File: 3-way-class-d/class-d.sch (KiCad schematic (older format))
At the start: 88 parts

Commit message: Make it a bit prettier
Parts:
- R? (x4): value 10 -> 3,3
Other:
- moved on the sheet: D?, Q?, R?
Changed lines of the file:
@@
 L R R?
 U 1 1 572BC593
-P 1400 3100
-F 0 "R?" V 1480 3100 50  0000 C CNN
-F 1 "0" V 1400 3100 50  0000 C CNN
-F 2 "" V 1330 3100 30  0000 C CNN
-F 3 "" H 1400 3100 30  0000 C CNN
-	1    1400 3100
+P 2150 3500
+F 0 "R?" V 2230 3500 50  0000 C CNN
+F 1 "0" V 2150 3500 50  0000 C CNN
+F 2 "" V 2080 3500 30  0000 C CNN
+F 3 "" H 2150 3500 30  0000 C CNN
+	1    2150 3500
 	0    1    1    0
 $EndComp
@@
 L GNDPWR #PWR?
 U 1 1 572BC8E0
-P 1100 3200
-F 0 "#PWR?" H 1100 3000 50  0001 C CNN
-F 1 "GNDPWR" H 1100 3070 50  0000 C CNN
-F 2 "" H 1100 3150 60  0000 C CNN
-F 3 "" H 1100 3150 60  0000 C CNN
-	1    1100 3200
+P 1850 3600
+F 0 "#PWR?" H 1850 3400 50  0001 C CNN
+F 1 "GNDPWR" H 1850 3470 50  0000 C CNN
+F 2 "" H 1850 3550 60  0000 C CNN
+F 3 "" H 1850 3550 60  0000 C CNN
+	1    1850 3600
 	0    1    1    0
 $EndComp
@@
 L R R?
 U 1 1 572BC605
-P 1400 3300
-F 0 "R?" V 1480 3300 50  0000 C CNN
-F 1 "22,1k" V 1400 3300 50  0000 C CNN
-F 2 "" V 1330 3300 30  0000 C CNN
-F 3 "" H 1400 3300 30  0000 C CNN
-	1    1400 3300
+P 2150 3700
+F 0 "R?" V 2230 3700 50  0000 C CNN
+F 1 "22,1k" V 2150 3700 50  0000 C CNN
+F 2 "" V 2080 3700 30  0000 C CNN
+F 3 "" H 2150 3700 30  0000 C CNN
+	1    2150 3700
 	0    1    1    0
 $EndComp
@@
 L BC857 Q?
 U 1 1 572BD9A9
-P 7250 4600
-F 0 "Q?" H 7450 4675 50  0000 L CNN
-F 1 "BC857" H 7450 4600 50  0000 L CNN
-F 2 "SOT-23" H 7450 4525 50  0000 L CIN
-F 3 "" H 7250 4600 50  0000 L CNN
-	1    7250 4600
+P 7300 4600
+F 0 "Q?" H 7500 4675 50  0000 L CNN
+F 1 "BC857" H 7500 4600 50  0000 L CNN
+F 2 "SOT-23" H 7500 4525 50  0000 L CIN
+F 3 "" H 7300 4600 50  0000 L CNN
+	1    7300 4600
 	1    0    0    -1
 $EndComp
@@
 L LED D?
 U 1 1 572BDA25
-P 7550 4400
-F 0 "D?" H 7550 4500 50  0000 C CNN
-F 1 "LED" H 7550 4300 50  0000 C CNN
-F 2 "" H 7550 4400 60  0000 C CNN
-F 3 "" H 7550 4400 60  0000 C CNN
-F 4 "Red" H 7550 4400 60  0001 C CNN "Color"
-	1    7550 4400
+P 7600 4400
+F 0 "D?" H 7600 4500 50  0000 C CNN
+F 1 "LED" H 7600 4300 50  0000 C CNN
+F 2 "" H 7600 4400 60  0000 C CNN
+F 3 "" H 7600 4400 60  0000 C CNN
+F 4 "Red" H 7600 4400 60  0001 C CNN "Color"
+	1    7600 4400
 	-1   0    0    1
 $EndComp
@@
 L GNDPWR #PWR?
 U 1 1 572BDA9C
-P 8050 4400
-F 0 "#PWR?" H 8050 4200 50  0001 C CNN
-F 1 "GNDPWR" H 8050 4270 50  0000 C CNN
-F 2 "" H 8050 4350 60  0000 C CNN
-F 3 "" H 8050 4350 60  0000 C CNN
-	1    8050 4400
+P 8100 4400
+F 0 "#PWR?" H 8100 4200 50  0001 C CNN
+F 1 "GNDPWR" H 8100 4270 50  0000 C CNN
+F 2 "" H 8100 4350 60  0000 C CNN
+F 3 "" H 8100 4350 60  0000 C CNN
+	1    8100 4400
 	0    -1   -1   0
 $EndComp
@@
 L R R?
 U 1 1 572BDBE6
-P 7900 4400
-F 0 "R?" V 7980 4400 50  0000 C CNN
-F 1 "332" V 7900 4400 50  0000 C CNN
-F 2 "" V 7830 4400 30  0000 C CNN
-F 3 "" H 7900 4400 30  0000 C CNN
-	1    7900 4400
+P 7950 4400
+F 0 "R?" V 8030 4400 50  0000 C CNN
+F 1 "332" V 7950 4400 50  0000 C CNN
+F 2 "" V 7880 4400 30  0000 C CNN
+F 3 "" H 7950 4400 30  0000 C CNN
+	1    7950 4400
 	0    1    -1   0
 $EndComp
@@
 L +3.3V #PWR?
 U 1 1 572BE227
-P 7350 4800
-F 0 "#PWR?" H 7350 4650 50  0001 C CNN
-F 1 "+3.3V" H 7350 4940 50  0000 C CNN
-F 2 "" H 7350 4800 60  0000 C CNN
-F 3 "" H 7350 4800 60  0000 C CNN
-	1    7350 4800
+P 7400 4800
+F 0 "#PWR?" H 7400 4650 50  0001 C CNN
+F 1 "+3.3V" H 7400 4940 50  0000 C CNN
+F 2 "" H 7400 4800 60  0000 C CNN
+F 3 "" H 7400 4800 60  0000 C CNN
+	1    7400 4800
 	-1   0    0    1
 $EndComp
-Text Notes 7150 4300 0    60   ~ 0
+Text Notes 7200 4300 0    60   ~ 0
 valid
-Text GLabel 7600 3700 2    60   Output ~ 0
+Text GLabel 7600 3500 2    60   Output ~ 0
 SUB-PWM+
-Text GLabel 7600 3900 2    60   Output ~ 0
+Text GLabel 7600 3650 2    60   Output ~ 0
 SUB-PWM-
-Text GLabel 7600 4100 2    60   Output ~ 0
+Text GLabel 7600 3800 2    60   Output ~ 0
 SUB-RESET
 $Comp
 L R R?
 U 1 1 572BECAA
-P 7250 4100
-F 0 "R?" V 7330 4100 50  0000 C CNN
-F 1 "47" V 7250 4100 50  0000 C CNN
-F 2 "" V 7180 4100 30  0000 C CNN
-F 3 "" H 7250 4100 30  0000 C CNN
-	1    7250 4100
+P 7250 3800
+F 0 "R?" V 7330 3800 50  0000 C CNN
+F 1 "47" V 7250 3800 50  0000 C CNN
+F 2 "" V 7180 3800 30  0000 C CNN
+F 3 "" H 7250 3800 30  0000 C CNN
+	1    7250 3800
 	0    -1   1    0
 $EndComp
@@
 Text GLabel 7650 5300 2    60   Input ~ 0
 MCLK
-Text GLabel 7650 5100 2    60   Output ~ 0
+Text GLabel 7600 3950 2    60   Input ~ 0
 BKND-ERR
 $Comp
@@
 Connection ~ 3850 5950
 Wire Wire Line
-	2850 4400 2450 4400
-Wire Wire Line
-	2450 4400 2450 3650
-Wire Wire Line
-	2450 3650 1800 3650
-Wire Wire Line
-	1800 3650 1800 1300
+	2450 4400 2850 4400
+Wire Wire Line
+	2450 1450 2450 4400
 Wire Notes Line
 	2400 1300 500  1300
@@
 Wire Notes Line
 	500  650  2400 650
-Wire Notes Line
-	2500 650  2500 1300
 Wire Wire Line
 	2050 6350 4050 6350
@@
 	2850 4500 2350 4500
 Wire Wire Line
-	1100 3200 1250 3200
+	1850 3600 2000 3600
 Wire Wire Line
 	2850 4300 2500 4300
 Wire Wire Line
-	1250 3100 1250 3300
-Connection ~ 1250 3200
-Wire Wire Line
-	1550 3300 2500 3300
-Wire Wire Line
-	2500 3300 2500 4300
+	2000 3500 2000 3700
+Connection ~ 2000 3600
 Wire Wire Line
 	2850 4200 2550 4200
-Wire Wire Line
-	2550 4200 2550 3100
-Wire Wire Line
-	2550 3100 1550 3100
-Wire Wire Line
-	5950 4600 7050 4600
 Connection ~ 6400 4250
 Wire Notes Line
-	7100 4200 7100 5000
-Wire Notes Line
-	7100 5000 8300 5000
-Wire Notes Line
-	8300 5000 8300 4200
-Wire Notes Line
-	8300 4200 7100 4200
-Wire Wire Line
-	6950 4100 6950 4600
-Connection ~ 6950 4600
-Wire Wire Line
-	5950 4500 6850 4500
-Wire Wire Line
-	6850 4500 6850 3900
-Wire Wire Line
-	6850 3900 7600 3900
-Wire Wire Line
-	7600 3700 6750 3700
-Wire Wire Line
-	6750 3700 6750 4400
+	7150 4200 7150 5000
+Wire Notes Line
+	7150 5000 8350 5000
+Wire Notes Line
+	8350 5000 8350 4200
+Wire Notes Line
+	8350 4200 7150 4200
+Wire Wire Line
+	6850 4500 5950 4500
+Wire Wire Line
+	6850 3650 6850 4500
+Wire Wire Line
+	6750 3500 6750 4400
 Wire Wire Line
 	6750 4400 5950 4400
-Wire Wire Line
-	7400 4100 7600 4100
-Wire Wire Line
-	6950 4100 7100 4100
 Wire Wire Line
 	6250 5000 6400 5000
@@
 Wire Wire Line
 	5950 4900 6650 4900
-Wire Wire Line
-	5950 4700 7050 4700
-Wire Wire Line
-	7050 4700 7050 5100
-Wire Wire Line
-	7050 5100 7650 5100
 Wire Wire Line
 	6950 4800 6950 5300
@@
 L +3.3V #PWR?
 U 1 1 572CDD5A
-P 1200 3600
-F 0 "#PWR?" H 1200 3450 50  0001 C CNN
-F 1 "+3.3V" H 1200 3740 50  0000 C CNN
-F 2 "" H 1200 3600 60  0000 C CNN
-F 3 "" H 1200 3600 60  0000 C CNN
-	1    1200 3600
+P 900 3600
+F 0 "#PWR?" H 900 3450 50  0001 C CNN
+F 1 "+3.3V" H 900 3740 50  0000 C CNN
+F 2 "" H 900 3600 60  0000 C CNN
+F 3 "" H 900 3600 60  0000 C CNN
+	1    900  3600
 	1    0    0    -1
 $EndComp
@@
 L R R?
 U 1 1 572CE04B
-P 1200 3750
-F 0 "R?" V 1280 3750 50  0000 C CNN
-F 1 "0" V 1200 3750 50  0000 C CNN
-F 2 "" V 1130 3750 30  0000 C CNN
-F 3 "" H 1200 3750 30  0000 C CNN
-	1    1200 3750
+P 900 3750
+F 0 "R?" V 980 3750 50  0000 C CNN
+F 1 "0" V 900 3750 50  0000 C CNN
+F 2 "" V 830 3750 30  0000 C CNN
+F 3 "" H 900 3750 30  0000 C CNN
+	1    900  3750
 	1    0    0    -1
 $EndComp
@@
 P 10250 1000
 F 0 "R?" V 10330 1000 50  0000 C CNN
-F 1 "10" V 10250 1000 50  0000 C CNN
+F 1 "3,3" V 10250 1000 50  0000 C CNN
 F 2 "" V 10180 1000 30  0000 C CNN
 F 3 "" H 10250 1000 30  0000 C CNN
@@
 P 10250 2200
 F 0 "R?" V 10330 2200 50  0000 C CNN
-F 1 "10" V 10250 2200 50  0000 C CNN
+F 1 "3,3" V 10250 2200 50  0000 C CNN
 F 2 "" V 10180 2200 30  0000 C CNN
 F 3 "" H 10250 2200 30  0000 C CNN
@@
 P 10250 3400
 F 0 "R?" V 10330 3400 50  0000 C CNN
-F 1 "10" V 10250 3400 50  0000 C CNN
+F 1 "3,3" V 10250 3400 50  0000 C CNN
 F 2 "" V 10180 3400 30  0000 C CNN
 F 3 "" H 10250 3400 30  0000 C CNN
@@
 P 10250 4550
 F 0 "R?" V 10330 4550 50  0000 C CNN
-F 1 "10" V 10250 4550 50  0000 C CNN
+F 1 "3,3" V 10250 4550 50  0000 C CNN
 F 2 "" V 10180 4550 30  0000 C CNN
 F 3 "" H 10250 4550 30  0000 C CNN
@@
 	8600 3000 8600 3250
 Wire Wire Line
-	5950 3500 8600 3500
-Wire Wire Line
-	8600 3500 8600 4400
-Connection ~ 5950 3500
+	8600 3350 8600 4400
 Wire Wire Line
 	6950 5300 7650 5300
+Wire Notes Line
+	8500 700  8500 5250
+Wire Notes Line
+	9750 700  9750 5250
+Wire Notes Line
+	8500 700  10400 700
+Wire Notes Line
+	10400 700  10400 5250
+Wire Notes Line
+	10400 5250 8500 5250
+Wire Wire Line
+	2450 1450 1800 1450
+Wire Wire Line
+	1800 1450 1800 1300
+Wire Notes Line
+	2400 650  2400 1300
+Wire Wire Line
+	2550 3500 2300 3500
+Wire Wire Line
+	2500 3700 2300 3700
+Wire Wire Line
+	2550 4200 2550 3500
+Wire Wire Line
+	2500 4300 2500 3700
+Wire Wire Line
+	8600 3350 5950 3350
+Connection ~ 5950 3350
+Wire Wire Line
+	7600 3500 6750 3500
+Wire Wire Line
+	6850 3650 7600 3650
+Wire Wire Line
+	7400 3800 7600 3800
+Wire Wire Line
+	7100 3800 6950 3800
+Wire Wire Line
+	5950 4600 7100 4600
+Wire Wire Line
+	6950 4600 6950 3800
+Wire Wire Line
+	5950 4700 7050 4700
+Wire Wire Line
+	7050 4700 7050 3950
+Wire Wire Line
+	7050 3950 7600 3950
+Connection ~ 6950 4600
 $EndSCHEMATC

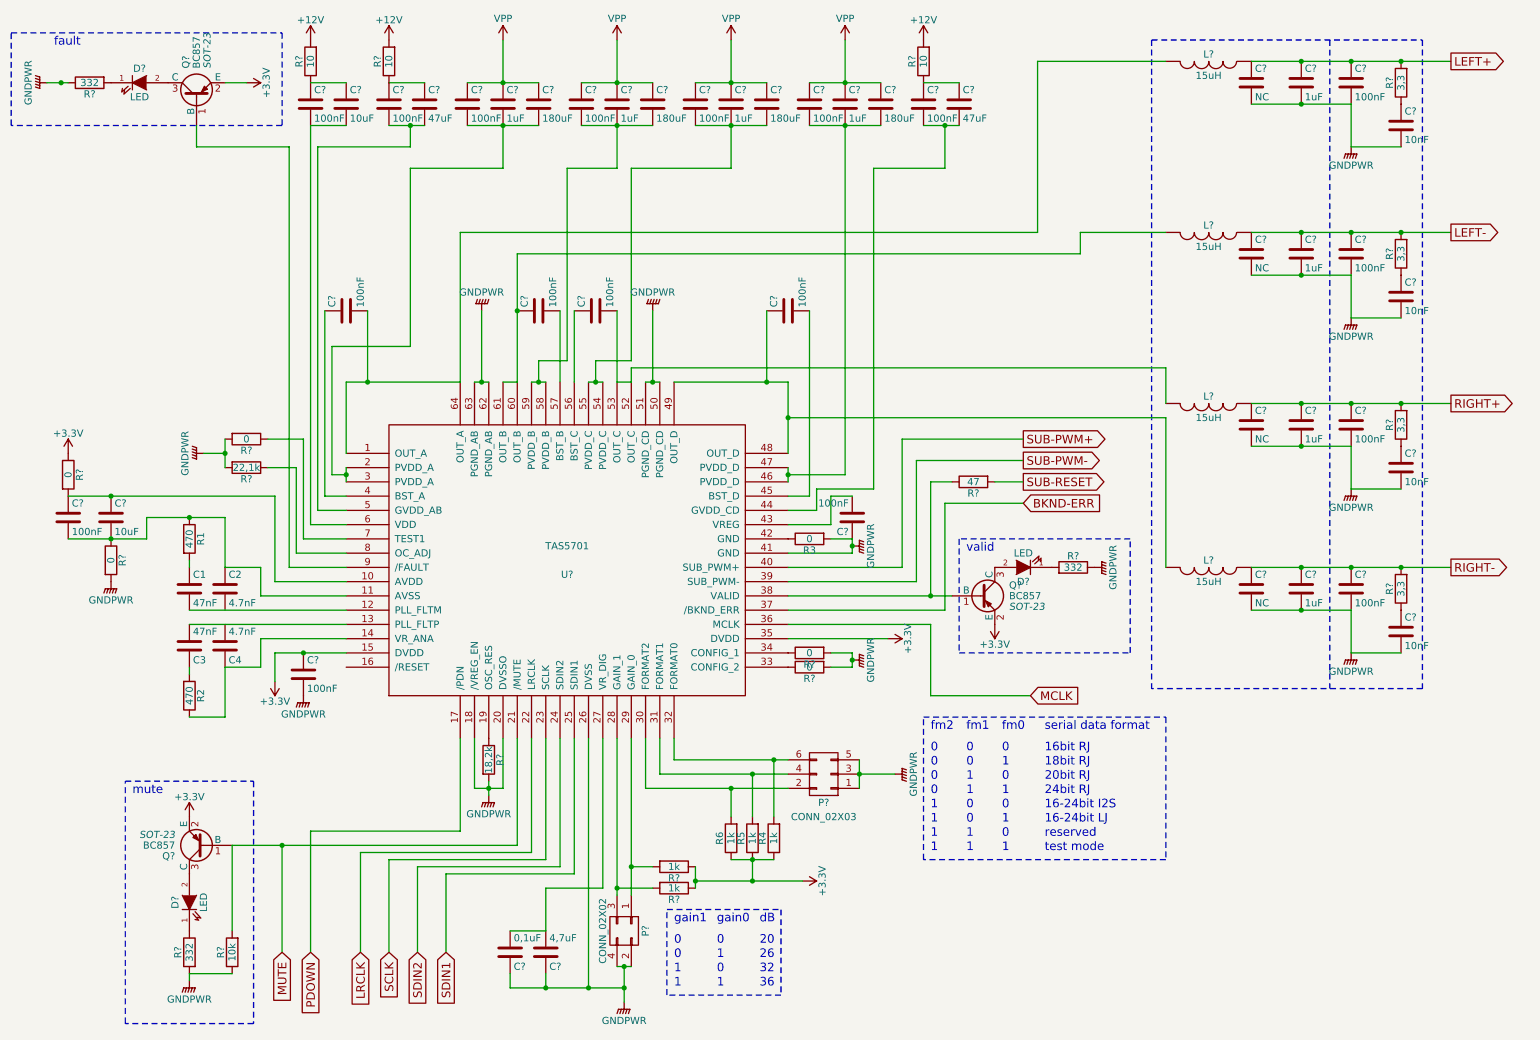
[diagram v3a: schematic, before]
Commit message: Schematics for power supplies from webench
Library reorganisation
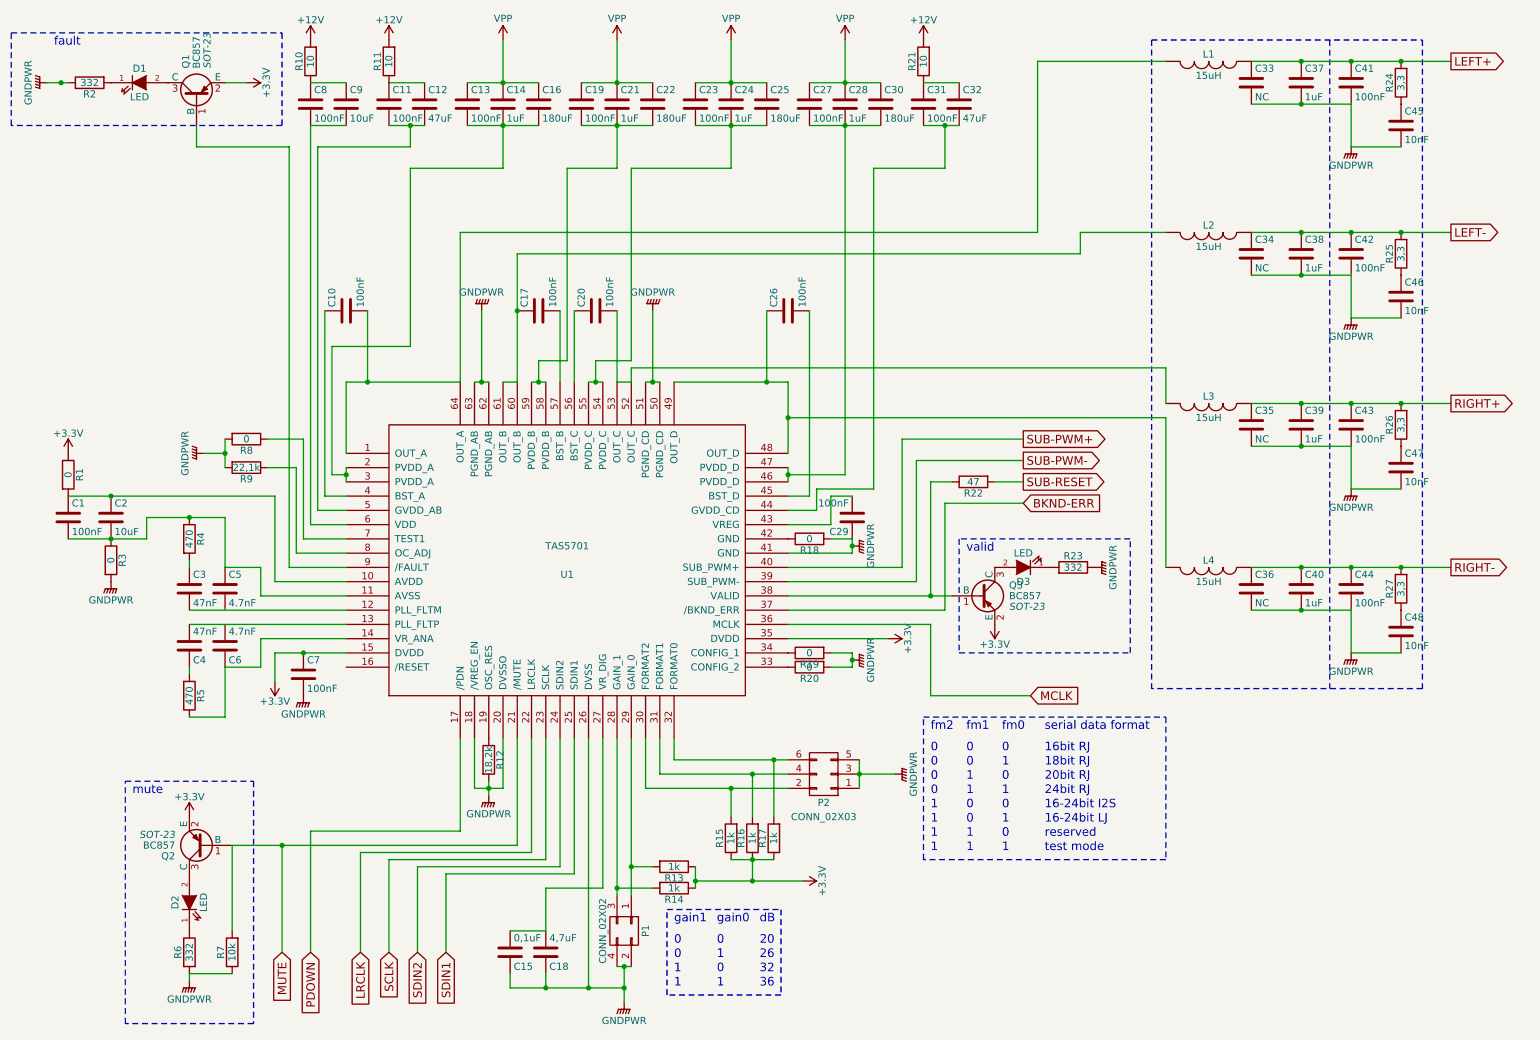
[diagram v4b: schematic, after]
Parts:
- gave numbers to parts that had none: 78
- renumbered C1 to C3, C3 to C4, C2 to C5, C4 to C6, R6 to R15, R5 to R16, R4 to R17, R3 to R18, R1 to R4, R2 to R5
